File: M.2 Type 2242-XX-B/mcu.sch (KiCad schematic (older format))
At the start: 30 parts, among them M1 MountingHole_Pad, U5 STM32F407VGTx, Y1 12MHz

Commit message: Add proper footprint to solder jumpers
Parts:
- SJ1, SJ2: footprint aausat:SolderJumper-3_P2.54mm_Bridged12_RoundedPad -> Jumper:SolderJumper-3_P1.3mm_Bridged12_RoundedPad1.0x1.5mm
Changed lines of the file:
@@
 F 0 "SJ2" H 5950 3555 50  0000 C CNN
 F 1 "BOOT1" H 5950 3464 50  0000 C CNN
-F 2 "aausat:SolderJumper-3_P2.54mm_Bridged12_RoundedPad" H 5950 3350 50  0001 C CNN
+F 2 "Jumper:SolderJumper-3_P1.3mm_Bridged12_RoundedPad1.0x1.5mm" H 5950 3350 50  0001 C CNN
 F 3 "~" H 5950 3350 50  0001 C CNN
 	1    5950 3350
@@
 F 0 "SJ1" H 1200 1855 50  0000 C CNN
 F 1 "BOOT0" H 1200 1764 50  0000 C CNN
-F 2 "aausat:SolderJumper-3_P2.54mm_Bridged12_RoundedPad" H 1200 1650 50  0001 C CNN
+F 2 "Jumper:SolderJumper-3_P1.3mm_Bridged12_RoundedPad1.0x1.5mm" H 1200 1650 50  0001 C CNN
 F 3 "~" H 1200 1650 50  0001 C CNN
 	1    1200 1650

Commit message: Initial placement, I think we are going for the STM32F103 instead
The LQPF-100 is simply too big
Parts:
- C24, C25, C28, C29, C30, C31, C32, C33: footprint Capacitor_SMD:C_0603_1608Metric -> Capacitor_SMD:C_0402_1005Metric
- R15, R16, R17, R18, R19, R20, R21: footprint Resistor_SMD:R_0603_1608Metric -> Resistor_SMD:R_0402_1005Metric
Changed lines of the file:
@@
 F 0 "C28" H 6615 1646 50  0000 L CNN
 F 1 "100n" H 6615 1555 50  0000 L CNN
-F 2 "Capacitor_SMD:C_0603_1608Metric" H 6538 1450 50  0001 C CNN
+F 2 "Capacitor_SMD:C_0402_1005Metric" H 6538 1450 50  0001 C CNN
 F 3 "~" H 6500 1600 50  0001 C CNN
 F 4 "CL10B104KO8WPNC" H 6500 1600 50  0001 C CNN "manf#"
@@
 F 0 "C29" H 6915 1646 50  0000 L CNN
 F 1 "100n" H 6915 1555 50  0000 L CNN
-F 2 "Capacitor_SMD:C_0603_1608Metric" H 6838 1450 50  0001 C CNN
+F 2 "Capacitor_SMD:C_0402_1005Metric" H 6838 1450 50  0001 C CNN
 F 3 "~" H 6800 1600 50  0001 C CNN
 F 4 "CL10B104KO8WPNC " H 6800 1600 50  0001 C CNN "manf#"
@@
 F 0 "C30" H 7215 1646 50  0000 L CNN
 F 1 "100n" H 7215 1555 50  0000 L CNN
-F 2 "Capacitor_SMD:C_0603_1608Metric" H 7138 1450 50  0001 C CNN
+F 2 "Capacitor_SMD:C_0402_1005Metric" H 7138 1450 50  0001 C CNN
 F 3 "~" H 7100 1600 50  0001 C CNN
 F 4 "CL10B104KO8WPNC" H -2800 -9000 50  0001 C CNN "manf#"
@@
 F 0 "C31" H 7515 1646 50  0000 L CNN
 F 1 "100n" H 7515 1555 50  0000 L CNN
-F 2 "Capacitor_SMD:C_0603_1608Metric" H 7438 1450 50  0001 C CNN
+F 2 "Capacitor_SMD:C_0402_1005Metric" H 7438 1450 50  0001 C CNN
 F 3 "~" H 7400 1600 50  0001 C CNN
 F 4 "CL10B104KO8WPNC" H -2800 -9000 50  0001 C CNN "manf#"
@@
 F 0 "C32" H 7815 1646 50  0000 L CNN
 F 1 "100n" H 7815 1555 50  0000 L CNN
-F 2 "Capacitor_SMD:C_0603_1608Metric" H 7738 1450 50  0001 C CNN
+F 2 "Capacitor_SMD:C_0402_1005Metric" H 7738 1450 50  0001 C CNN
 F 3 "~" H 7700 1600 50  0001 C CNN
 F 4 "CL10B104KO8WPNC" H -2800 -9000 50  0001 C CNN "manf#"
@@
 F 0 "C33" H 8115 1646 50  0000 L CNN
 F 1 "100n" H 8115 1555 50  0000 L CNN
-F 2 "Capacitor_SMD:C_0603_1608Metric" H 8038 1450 50  0001 C CNN
+F 2 "Capacitor_SMD:C_0402_1005Metric" H 8038 1450 50  0001 C CNN
 F 3 "~" H 8000 1600 50  0001 C CNN
 F 4 "CL10B104KO8WPNC" H -2800 -9000 50  0001 C CNN "manf#"
@@
 F 0 "R17" H 9520 2046 50  0000 L CNN
 F 1 "10K" H 9520 1955 50  0000 L CNN
-F 2 "Resistor_SMD:R_0603_1608Metric" V 9380 2000 50  0001 C CNN
+F 2 "Resistor_SMD:R_0402_1005Metric" V 9380 2000 50  0001 C CNN
 F 3 "~" H 9450 2000 50  0001 C CNN
 	1    9450 2000
@@
 F 0 "R21" H 10720 1746 50  0000 L CNN
 F 1 "10K" H 10720 1655 50  0000 L CNN
-F 2 "Resistor_SMD:R_0603_1608Metric" V 10580 1700 50  0001 C CNN
+F 2 "Resistor_SMD:R_0402_1005Metric" V 10580 1700 50  0001 C CNN
 F 3 "~" H 10650 1700 50  0001 C CNN
 	1    10650 1700
@@
 F 0 "R15" V 7950 3800 50  0000 C CNN
 F 1 "20R" V 7850 3800 50  0000 C CNN
-F 2 "Resistor_SMD:R_0603_1608Metric" V 7780 3800 50  0001 C CNN
+F 2 "Resistor_SMD:R_0402_1005Metric" V 7780 3800 50  0001 C CNN
 F 3 "~" H 7850 3800 50  0001 C CNN
 	1    7850 3800
@@
 F 0 "R16" V 7950 3950 50  0000 C CNN
 F 1 "20R" V 7850 3950 50  0000 C CNN
-F 2 "Resistor_SMD:R_0603_1608Metric" V 7780 3950 50  0001 C CNN
+F 2 "Resistor_SMD:R_0402_1005Metric" V 7780 3950 50  0001 C CNN
 F 3 "~" H 7850 3950 50  0001 C CNN
 	1    7850 3950
@@
 F 0 "C24" V 1148 2700 50  0000 C CNN
 F 1 "27pF" V 1239 2700 50  0000 C CNN
-F 2 "Capacitor_SMD:C_0603_1608Metric" H 1438 2550 50  0001 C CNN
+F 2 "Capacitor_SMD:C_0402_1005Metric" H 1438 2550 50  0001 C CNN
 F 3 "~" H 1400 2700 50  0001 C CNN
 	1    1400 2700
@@
 F 0 "C25" V 1560 3100 50  0000 C CNN
 F 1 "27pF" V 1651 3100 50  0000 C CNN
-F 2 "Capacitor_SMD:C_0603_1608Metric" H 1438 2950 50  0001 C CNN
+F 2 "Capacitor_SMD:C_0402_1005Metric" H 1438 2950 50  0001 C CNN
 F 3 "~" H 1400 3100 50  0001 C CNN
 	1    1400 3100
@@
 F 0 "R18" H 9520 3296 50  0000 L CNN
 F 1 "10K" H 9520 3205 50  0000 L CNN
-F 2 "Resistor_SMD:R_0603_1608Metric" V 9380 3250 50  0001 C CNN
+F 2 "Resistor_SMD:R_0402_1005Metric" V 9380 3250 50  0001 C CNN
 F 3 "~" H 9450 3250 50  0001 C CNN
 	1    9450 3250
@@
 F 0 "R20" H 10320 1846 50  0000 L CNN
 F 1 "10K" H 10320 1755 50  0000 L CNN
-F 2 "Resistor_SMD:R_0603_1608Metric" V 10180 1800 50  0001 C CNN
+F 2 "Resistor_SMD:R_0402_1005Metric" V 10180 1800 50  0001 C CNN
 F 3 "~" H 10250 1800 50  0001 C CNN
 	1    10250 1800
@@
 F 0 "R19" H 9920 1946 50  0000 L CNN
 F 1 "10K" H 9920 1855 50  0000 L CNN
-F 2 "Resistor_SMD:R_0603_1608Metric" V 9780 1900 50  0001 C CNN
+F 2 "Resistor_SMD:R_0402_1005Metric" V 9780 1900 50  0001 C CNN
 F 3 "~" H 9850 1900 50  0001 C CNN
 	1    9850 1900

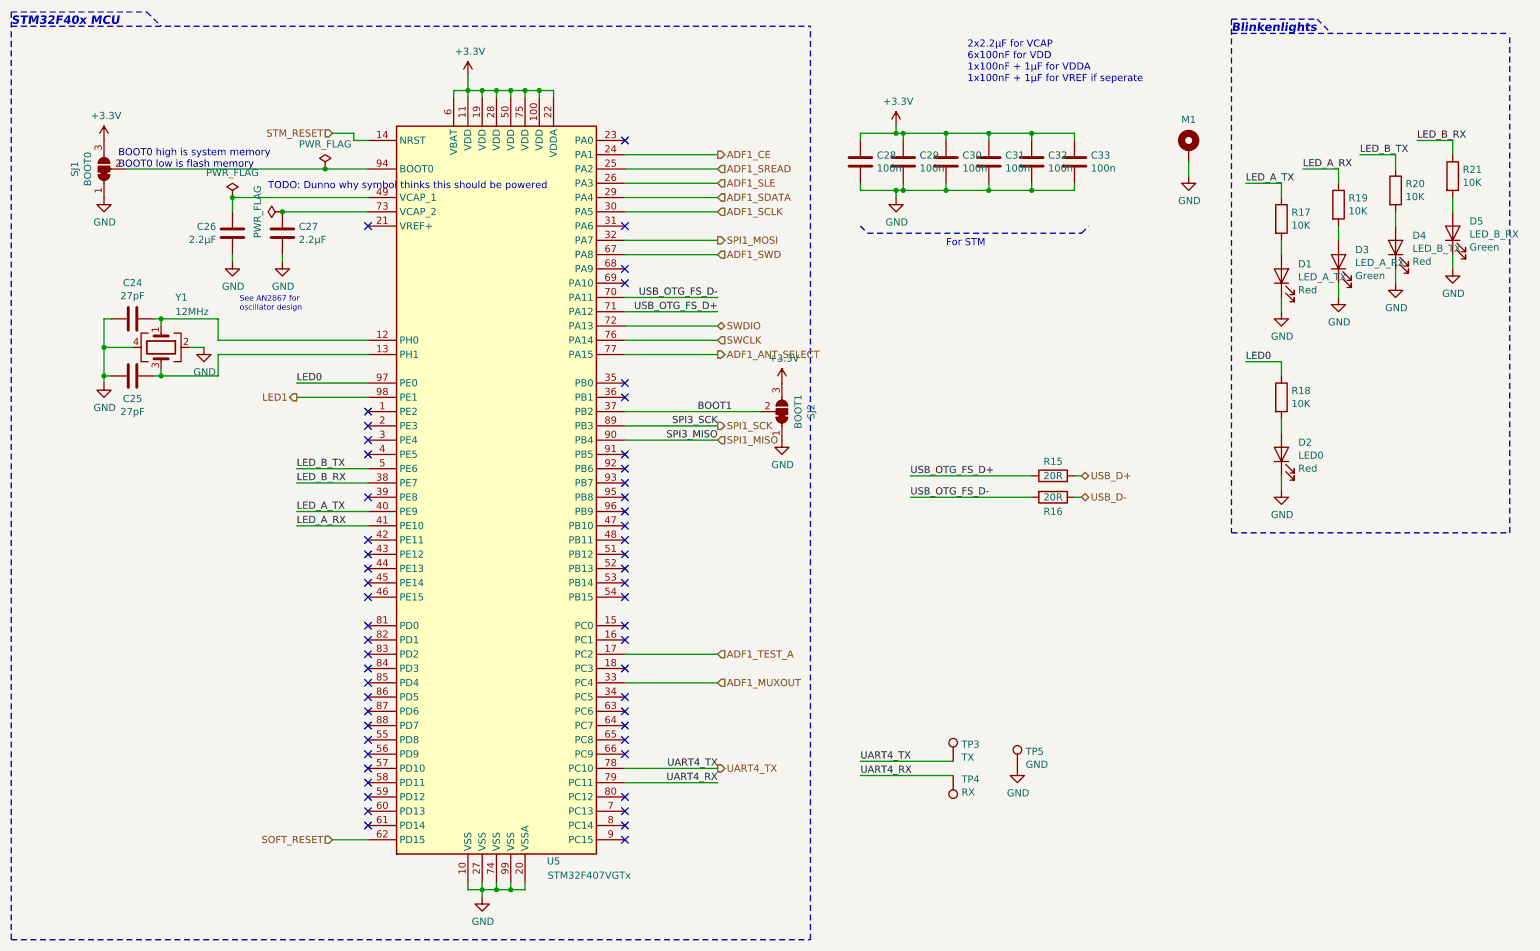
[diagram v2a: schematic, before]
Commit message: Schematic updated to STM32F103
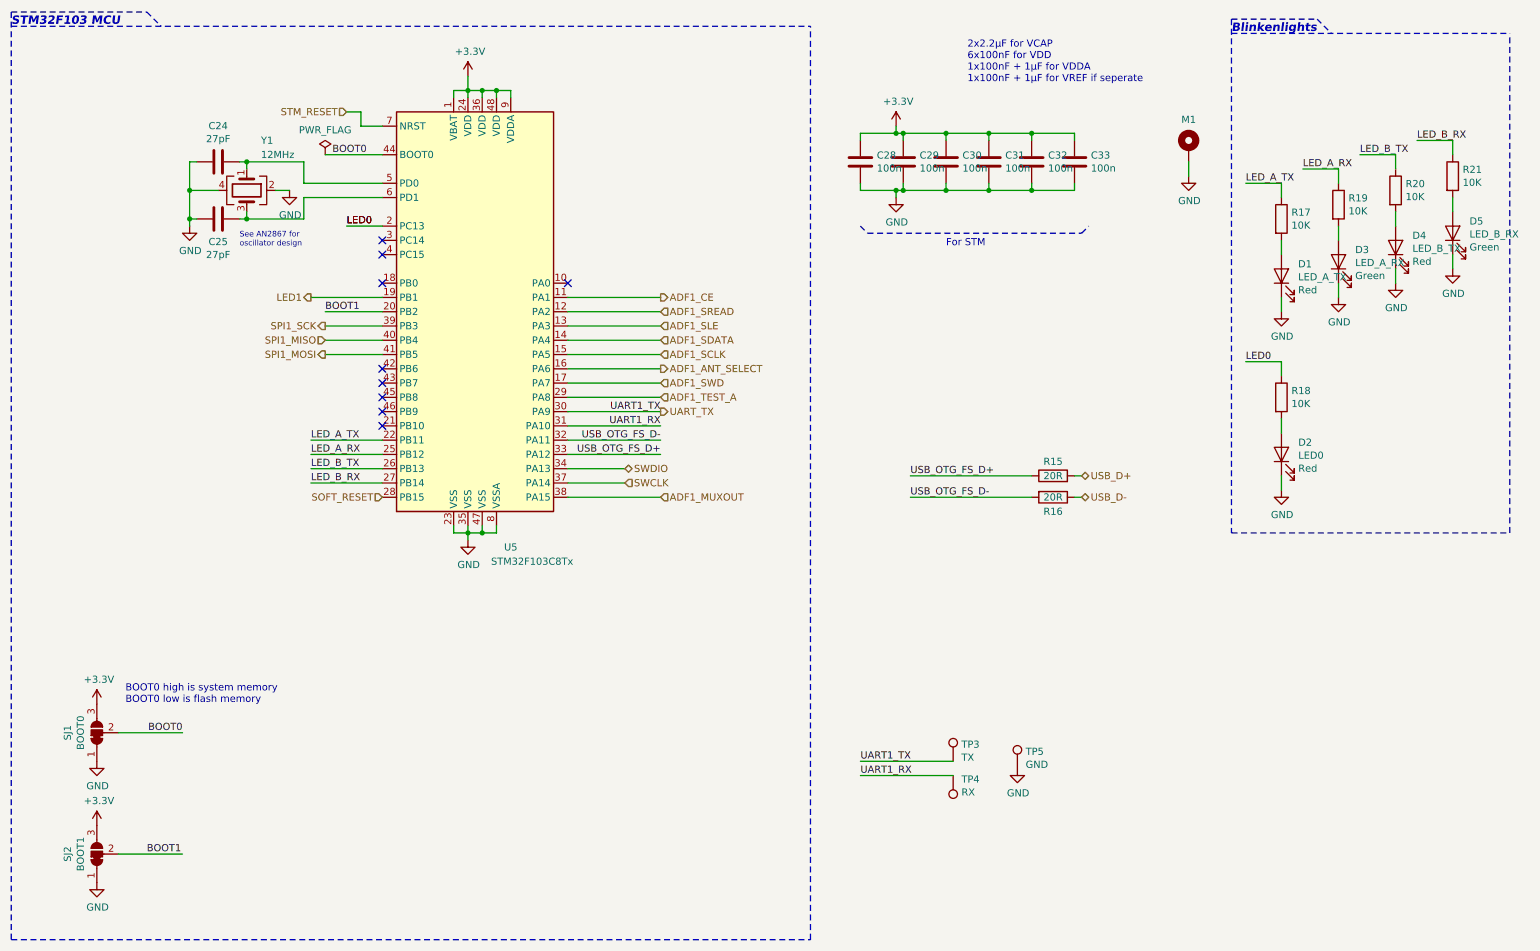
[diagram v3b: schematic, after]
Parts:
- removed C26, C27: 2.2µF, Capacitor_Tantalum_SMD:CP_EIA-3216-18_Kemet-A, symbol Device:C
- removed U5: STM32F407VGTx, Package_QFP:LQFP-100_14x14mm_P0.5mm, symbol MCU_ST_STM32F4:STM32F407VGTx
- added U5: STM32F103C8Tx, Package_QFP:LQFP-48_7x7mm_P0.5mm, symbol MCU_ST_STM32F1:STM32F103C8Tx
- C24, C25, C28, C29, C30, C31, C32, C33: footprint Capacitor_SMD:C_0402_1005Metric -> Capacitor_SMD:C_0603_1608Metric
- R15, R16, R17, R18, R19, R20, R21: footprint Resistor_SMD:R_0402_1005Metric -> Resistor_SMD:R_0603_1608Metric
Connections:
- net +3V3: now also U5.1 (VBAT), U5.24 (VDD), U5.36 (VDD), U5.48 (VDD), U5.9 (VDDA)
- net ADF1_ANT_SELECT: now also U5.16 (PA6)
- net ADF1_CE: now also U5.11 (PA1)
- net ADF1_MUXOUT: now also U5.38 (PA15)
- net ADF1_SCLK: now also U5.15 (PA5)
- net ADF1_SDATA: now also U5.14 (PA4)
- net ADF1_SLE: now also U5.13 (PA3)
- net ADF1_SREAD: now also U5.12 (PA2)
- net ADF1_SWD: now also U5.17 (PA7)
- net ADF1_TEST_A: now also U5.29 (PA8)
- net BOOT1: now also U5.20 (PB2)
- net GND: now also U5.23 (VSS), U5.35 (VSS), U5.47 (VSS), U5.8 (VSSA)
- net LED0: now also U5.2 (PC13)
- net LED1: now also U5.19 (PB1)
- net LED_A_RX: now also U5.25 (PB12)
- net LED_A_TX: now also U5.22 (PB11)
- net LED_B_RX: now also U5.27 (PB14)
- net LED_B_TX: now also U5.26 (PB13)
- net SOFT_RESET: now also U5.28 (PB15)
- net SPI1_MISO: now also U5.40 (PB4)
- net SPI1_MOSI: now also U5.41 (PB5)
- net SPI1_SCK: now also U5.39 (PB3)
- net STM_RESET: now also U5.7 (NRST)
- net SWCLK: now also U5.37 (PA14)
- net SWDIO: now also U5.34 (PA13)
- net USB_OTG_FS_D+: now also U5.33 (PA12)
- net USB_OTG_FS_D-: now also U5.32 (PA11)
- net at C24.1, Y1.1: now also U5.5 (PD0)
- net at C25.1, Y1.3: now also U5.6 (PD1)
- net BOOT0: now reaches SJ1.2 (C)
- net BOOT0: now also U5.44 (BOOT0)
- net UART4_RX renamed UART1_RX
- net UART1_RX: now also U5.31 (PA10)
- net UART4_TX renamed UART_TX
- net UART_TX: now also U5.30 (PA9)
- no-connect marks 55 -> 9
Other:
- note added: "STM32F103 MCU"
- note removed: "STM32F40x MCU"
- note removed: "TODO: Dunno why symbol thinks this should be powered"
- moved on the sheet: C24, C25, SJ1, Y1

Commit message: Almost everything placed
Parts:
- TP201: renamed from TP3; footprint TestPoint:TestPoint_Pad_D1.5mm -> aausat:TestPad
- TP202: renamed from TP4; footprint TestPoint:TestPoint_Pad_D1.5mm -> aausat:TestPad
- TP203: renamed from TP5; footprint TestPoint:TestPoint_Pad_D1.5mm -> aausat:TestPad
- renumbered C24 to C201, C25 to C202, C28 to C203, C29 to C204, C30 to C205, C31 to C206, C32 to C207, C33 to C208, D1 to D201, D2 to D202, D3 to D203, D4 to D204, D5 to D205, M1 to M201, R15 to R201, R16 to R202, R17 to R203, R18 to R204, R19 to R205, R20 to R206, R21 to R207, SJ1 to SJ201, SJ2 to SJ202, U5 to U201, Y1 to Y201
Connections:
- net USB_D-: now also R202.2; no longer R202.1
- net USB_OTG_FS_D-: now also R202.1; no longer R202.2
